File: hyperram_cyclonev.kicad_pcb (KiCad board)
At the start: 2 copper layers, 70.1 x 89.7 mm, 65 parts, among them IC1 AP63205WU, IC2 TXB0108PWR, IC3 S26KL128SDABHI020, IC4 W25Q32JVSSIQ_TR, IC5 S27KL0641DABHI020, J1 ASP-122952-01, J2 HDMI_A, J3 Conn_02x10_Odd_Even, J4 Conn_02x06_Odd_Even, J5 Conn_02x06_Top_Bottom, J6 Conn_02x06_Top_Bottom, J7 Conn_02x06_Top_Bottom, Q1 BSS138, Q2 BSS138

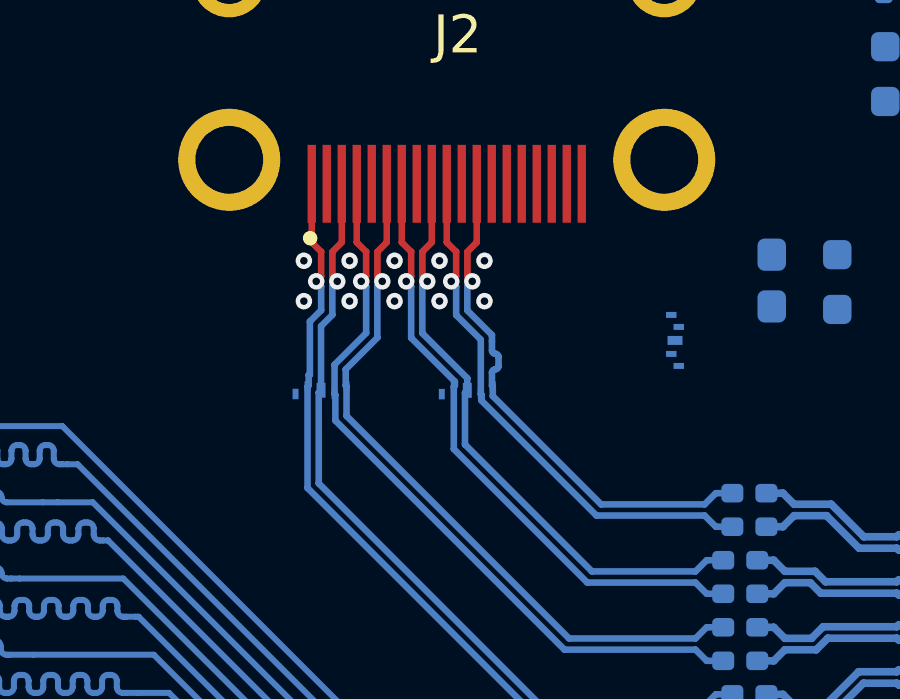
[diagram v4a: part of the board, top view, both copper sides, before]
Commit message: Updated PCB with latest fixes in schematic related to SESD Series TVS Diode Array
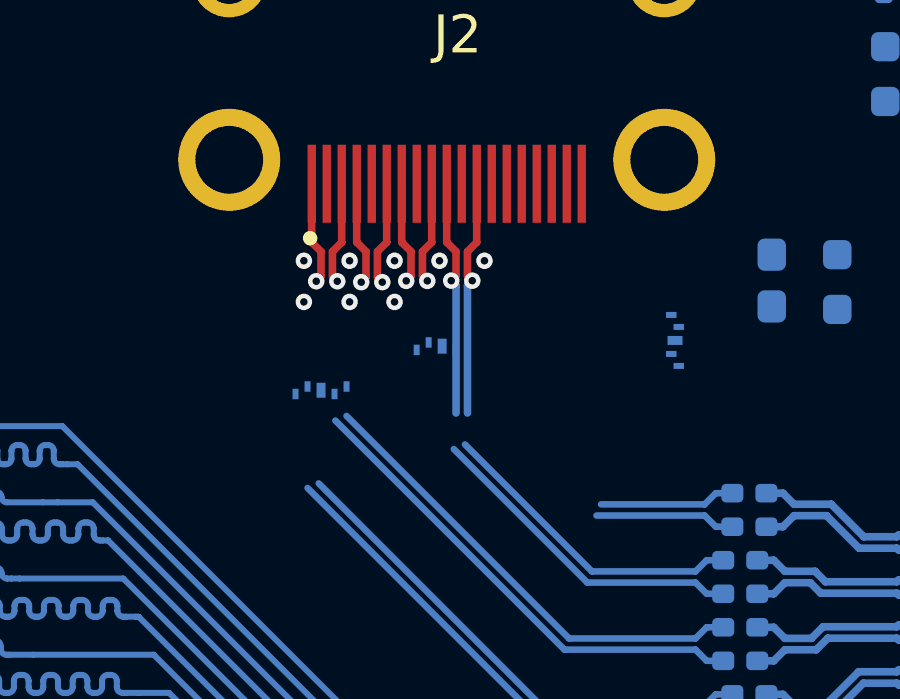
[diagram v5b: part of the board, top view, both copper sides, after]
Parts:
- moved D1 1.69 mm to (203.1, 80.1)
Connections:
- D1 pad 2: /xhdmi_d0+ -> /xhdmi_d0-
- D1 pad 3: GND -> /xhdmi_d0+
- D1 pad 5: /xhdmi_d0- -> GND
- D2 pad 2: /cec -> /ddc_clk
- D2 pad 3: GND -> /cec
- D2 pad 5: /ddc_clk -> GND
- D4 pad 2: /xhdmi_d2+ -> /xhdmi_d2-
- D4 pad 3: GND -> /xhdmi_d2+
- D4 pad 5: /xhdmi_d2- -> GND
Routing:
- net /xhdmi_d2+: track 28.1 -> 20.9 mm
- net /xhdmi_d2-: track 27.4 -> 20.5 mm
- net /xhdmi_d0+: track 20.7 -> 14.4 mm
- net /xhdmi_d0-: track 20.1 -> 13.9 mm
- net /xhdmi_clk+: track 17.9 -> 12.6 mm
- net /xhdmi_d1+: track 24.9 -> 19.7 mm
- net /xhdmi_clk-: track 17.6 -> 12.4 mm
- net /xhdmi_d1-: track 24.2 -> 19.3 mm
- net GND: vias 25 -> 23
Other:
- copper layers 2 -> 4

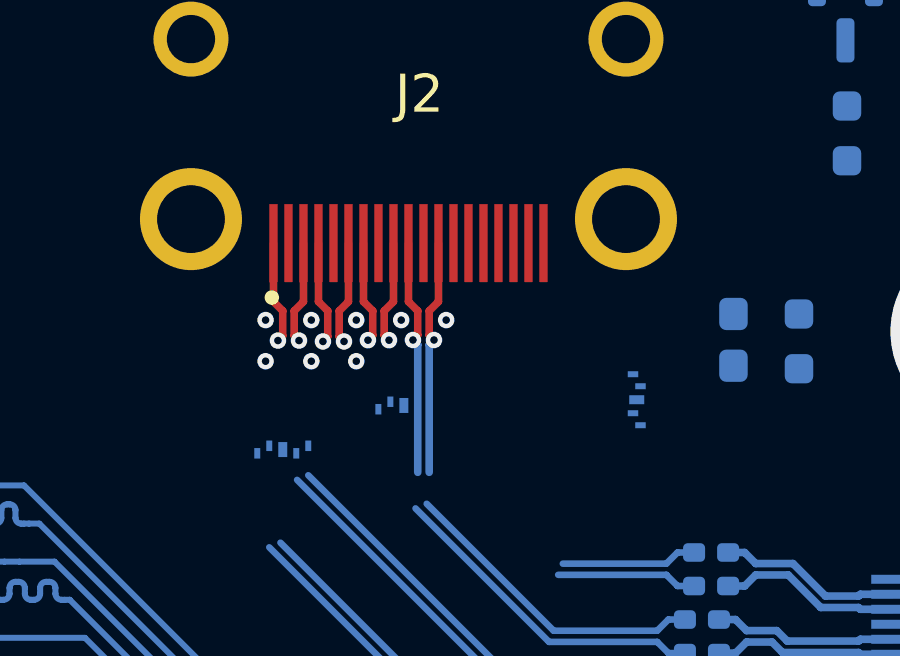
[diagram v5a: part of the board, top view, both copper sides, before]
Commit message: Updated SESD Series TVS Diode Arrays on PCB
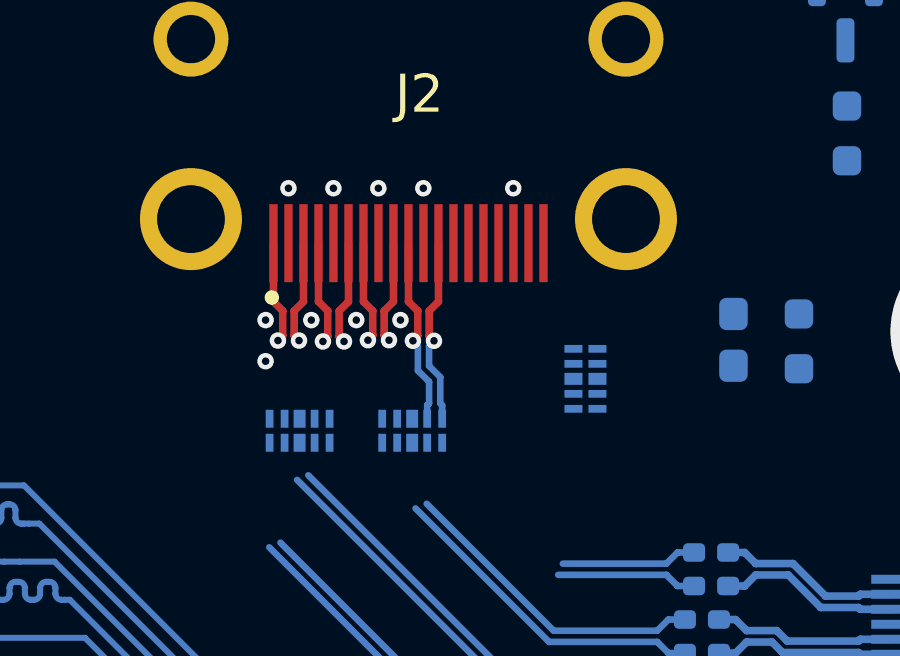
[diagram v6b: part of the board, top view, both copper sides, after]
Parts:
- D1, D2, D4: value SESD0802Q4UG-0020-090 -> SESD1004Q4UG-0020-090; footprint hyperram_cyclonev:SESD0802Q4UG0020090 -> hyperram_cyclonev:SESD1004Q4UG0020090
- moved D2 1.85 mm to (209.2, 79.3)
- moved D1 0.89 mm to (203.4, 81.0)
- moved D4 0.84 mm to (199.6, 81.0)
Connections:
- D1 pad 2: /xhdmi_d0- -> /xhdmi_clk+
- D1 pad 3: /xhdmi_d0+ -> GND
- D1 pad 4: /xhdmi_clk+ -> /xhdmi_d0-
- D1 pad 5: GND -> /xhdmi_d0+
- D2 pad 2: /ddc_clk -> /ddc_dat
- D2 pad 3: /cec -> GND
- D2 pad 4: /ddc_dat -> /ddc_clk
- D2 pad 5: GND -> /cec
- D4 pad 2: /xhdmi_d2- -> /xhdmi_d1+
- D4 pad 3: /xhdmi_d2+ -> GND
- D4 pad 4: /xhdmi_d1+ -> /xhdmi_d2-
- D4 pad 5: GND -> /xhdmi_d2+
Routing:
- net /xhdmi_clk+: track 12.6 -> 11.0 mm
- net /xhdmi_clk-: track 12.4 -> 10.8 mm
- net GND: vias 23 -> 25

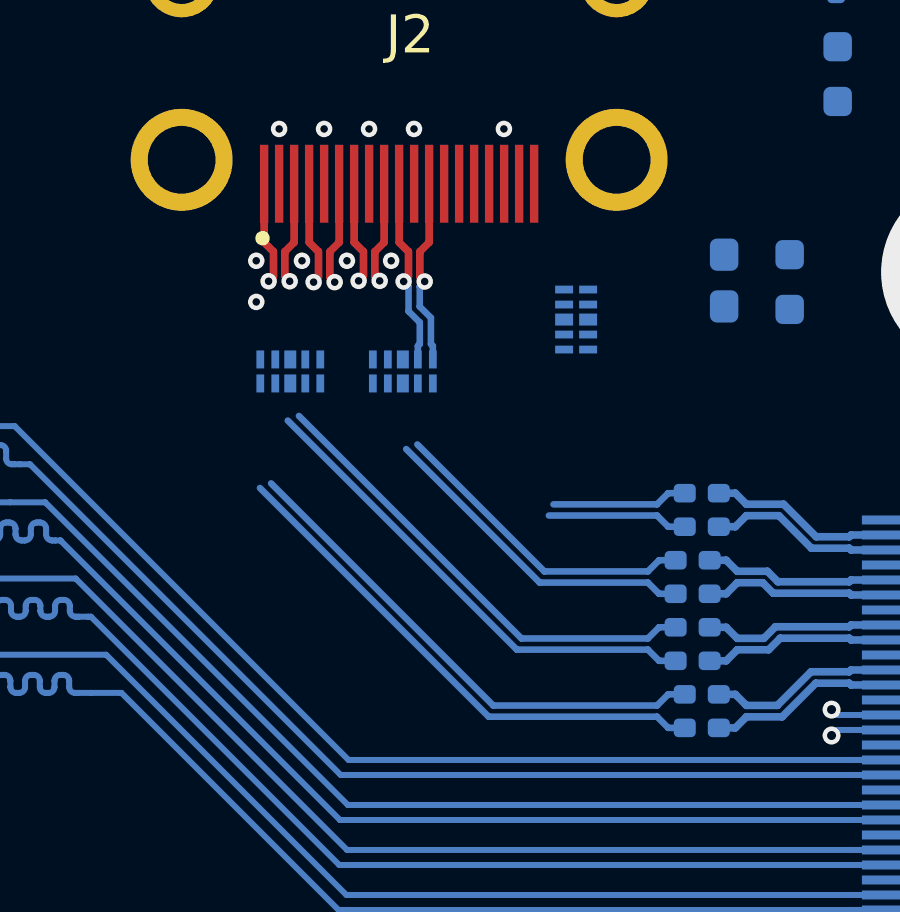
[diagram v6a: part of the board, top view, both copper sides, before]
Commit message: Routed HDMI differential pairs with intra-pair lenght matching
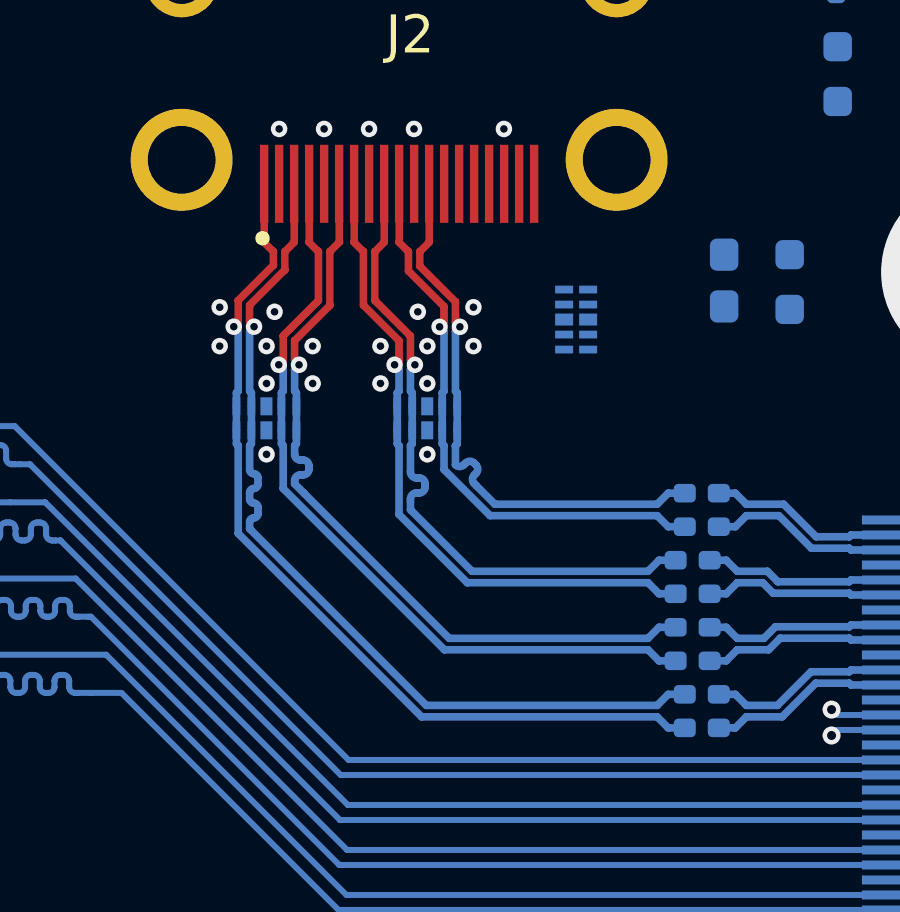
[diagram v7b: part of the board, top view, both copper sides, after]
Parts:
- moved D1 1.76 mm to (204.2, 82.5)
- moved D4 1.75 mm to (198.8, 82.5)
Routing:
- net /xhdmi_d2-: track 20.5 -> 30.0 mm
- net /xhdmi_d2+: track 20.9 -> 30.0 mm
- net /xhdmi_clk-: track 10.8 -> 19.1 mm
- net /xhdmi_d0-: track 13.9 -> 22.1 mm
- net /xhdmi_clk+: track 11.0 -> 19.1 mm
- net /xhdmi_d0+: track 14.4 -> 22.1 mm
- net /xhdmi_d1-: track 19.3 -> 26.4 mm
- net /xhdmi_d1+: track 19.7 -> 26.4 mm
- net GND: vias 25 -> 36

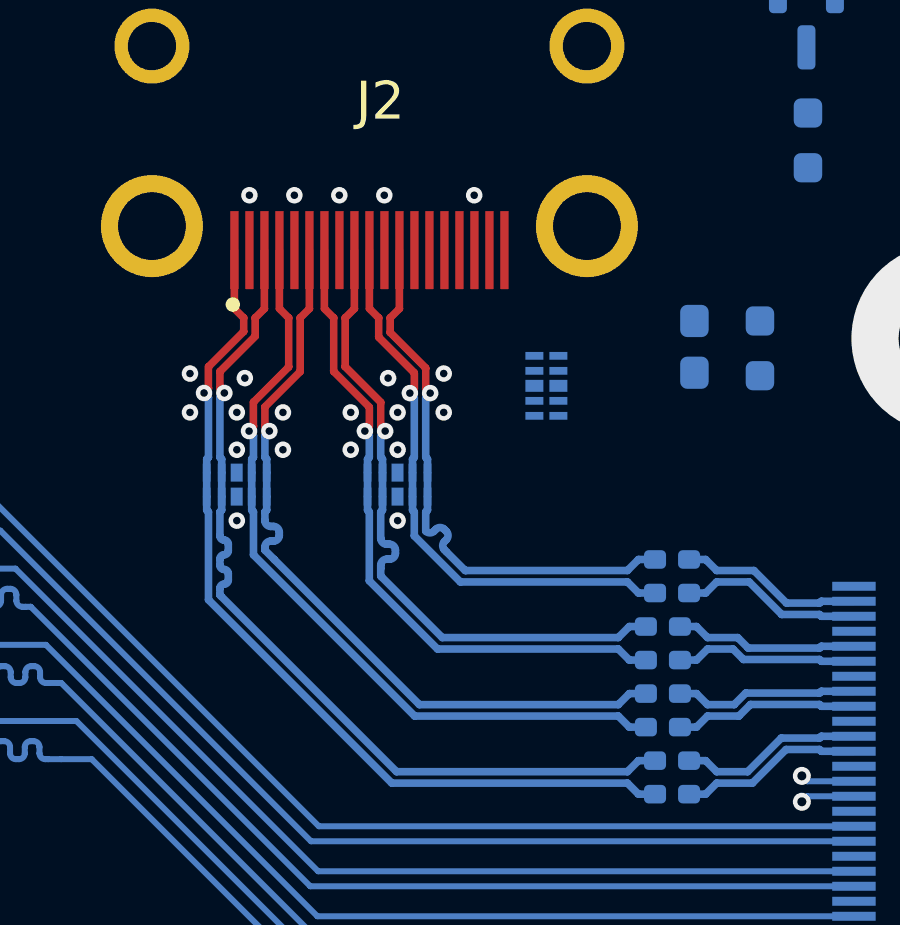
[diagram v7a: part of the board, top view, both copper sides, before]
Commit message: Equalized lenghts of HDMI differential pairs.
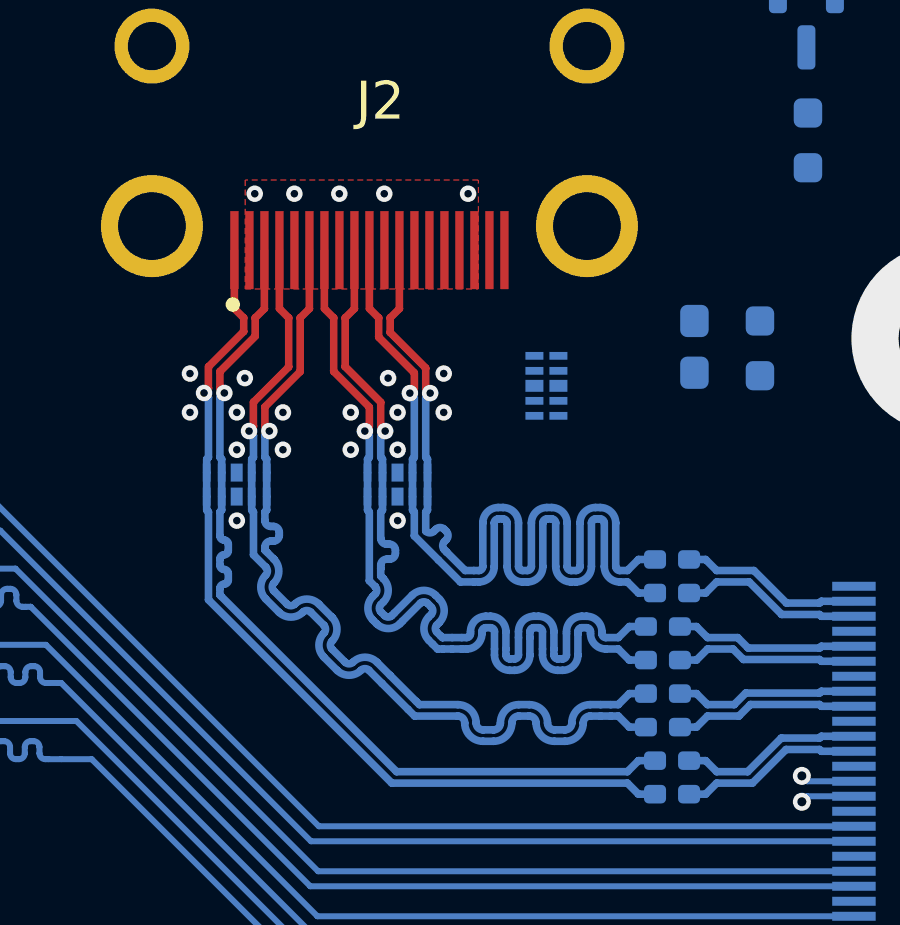
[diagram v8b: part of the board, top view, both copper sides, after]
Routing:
- net /xhdmi_clk+: track 19.1 -> 29.9 mm
- net /xhdmi_clk-: track 19.1 -> 29.9 mm
- net /xhdmi_d0+: track 22.1 -> 29.8 mm
- net /xhdmi_d0-: track 22.1 -> 29.8 mm
- net /xhdmi_d1+: track 26.4 -> 29.8 mm
- net /xhdmi_d1-: track 26.4 -> 29.7 mm
- added copper zone on F.Cu, net GND
